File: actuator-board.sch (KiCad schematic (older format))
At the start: 29 parts, among them J5 SWD/DEBUG, J6 BATTERY, J7 CAN, J8 CAN, U1 STM32F302K8U6, U2 MCP1703, U3 MAX3051, X1 16MHz 10ppm

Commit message: layout: power electronics, more components on F.Cu layer
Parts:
- U2: footprint Package_TO_SOT_SMD:SOT-23_Handsoldering -> Package_TO_SOT_SMD:SOT-23
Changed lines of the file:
@@
 F 0 "U2" H 9100 1200 60  0000 C CNN
 F 1 "MCP1703" H 8800 1200 60  0000 C CNN
-F 2 "Package_TO_SOT_SMD:SOT-23_Handsoldering" H 8750 1450 60  0001 C CNN
+F 2 "Package_TO_SOT_SMD:SOT-23" H 8750 1450 60  0001 C CNN
 F 3 "" H 8750 1450 60  0000 C CNN
 F 4 "MCP1703T-3302E/CBCT-ND" H 8850 1300 50  0001 C CNN "digikey#"

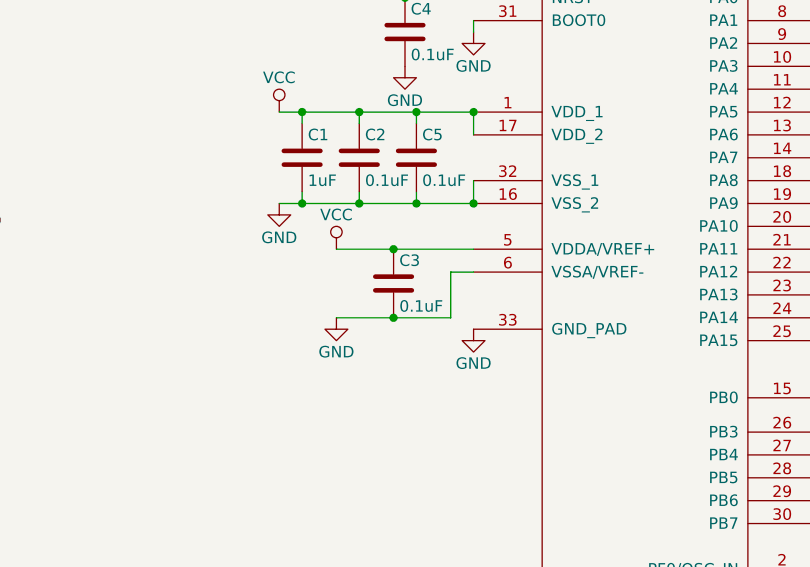
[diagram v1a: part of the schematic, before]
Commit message: HTSSOP motor driver, component arrangment, added MCU capacitor
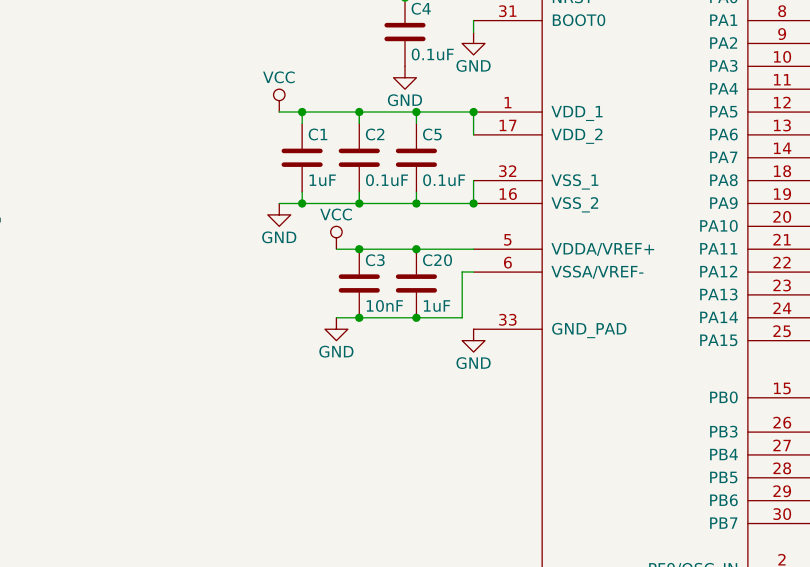
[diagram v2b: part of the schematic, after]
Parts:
- added C20: 1uF, Capacitor_SMD:C_0603_1608Metric, symbol Device:C
- C3: value 0.1uF -> 10nF
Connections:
- net GND: now also C20.2
- net VCC: now also C20.1
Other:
- moved on the sheet: C3
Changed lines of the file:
@@
-$EndComp
-$Comp
-L Device:C C3
-U 1 1 56D6293B
-P 3500 4350
-F 0 "C3" H 3525 4450 50  0000 L CNN
-F 1 "0.1uF" H 3525 4250 50  0000 L CNN
-F 2 "Capacitor_SMD:C_0603_1608Metric" H 3538 4200 50  0001 C CNN
-F 3 "" H 3500 4350 50  0000 C CNN
-	1    3500 4350
-	1    0    0    -1
 $EndComp
 $Comp
@@
 	2150 1600 1750 1600
 Wire Wire Line
-	3750 4300 3750 4500
-Wire Wire Line
-	3850 4300 3750 4300
+	3800 4300 3800 4500
+Wire Wire Line
+	3850 4300 3800 4300
 Connection ~ 3350 4000
 Wire Wire Line
@@
 Wire Wire Line
 	3400 3100 3550 3100
-Wire Wire Line
-	3250 4500 3500 4500
-Wire Wire Line
-	3250 4200 3500 4200
 Wire Wire Line
 	5350 3700 5450 3700
@@
 	1    0    0    -1
 $EndComp
-Connection ~ 3500 4200
-Wire Wire Line
-	3500 4200 3850 4200
-Connection ~ 3500 4500
-Wire Wire Line
-	3500 4500 3750 4500
 $Comp
 L power:GND #PWR012
@@
 Text Label 5450 3100 0    60   ~ 0
 ANALOG1
+$Comp
+L Device:C C20
+U 1 1 5E52DAB3
+P 3600 4350
+F 0 "C20" H 3625 4450 50  0000 L CNN
+F 1 "1uF" H 3625 4250 50  0000 L CNN
+F 2 "Capacitor_SMD:C_0603_1608Metric" H 3638 4200 50  0001 C CNN
+F 3 "" H 3600 4350 50  0000 C CNN
+	1    3600 4350
+	1    0    0    -1
+$EndComp
+Connection ~ 3600 4200
+Wire Wire Line
+	3600 4200 3850 4200
+Connection ~ 3600 4500
+Wire Wire Line
+	3600 4500 3800 4500
+Wire Wire Line
+	3250 4500 3350 4500
+Connection ~ 3350 4500
+Wire Wire Line
+	3350 4500 3600 4500
+Wire Wire Line
+	3250 4200 3350 4200
+Connection ~ 3350 4200
+Wire Wire Line
+	3350 4200 3600 4200
+$Comp
+L Device:C C3
+U 1 1 56D6293B
+P 3350 4350
+F 0 "C3" H 3375 4450 50  0000 L CNN
+F 1 "10nF" H 3375 4250 50  0000 L CNN
+F 2 "Capacitor_SMD:C_0603_1608Metric" H 3388 4200 50  0001 C CNN
+F 3 "" H 3350 4350 50  0000 C CNN
+	1    3350 4350
+	1    0    0    -1
+$EndComp
 $EndSCHEMATC

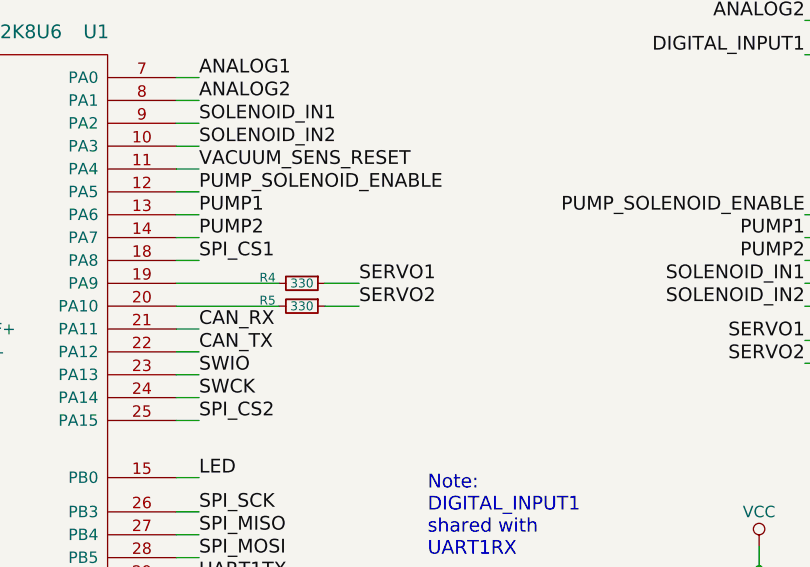
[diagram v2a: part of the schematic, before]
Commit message: Silk screen doc, ground vias, exchange servo 1 <-> 2
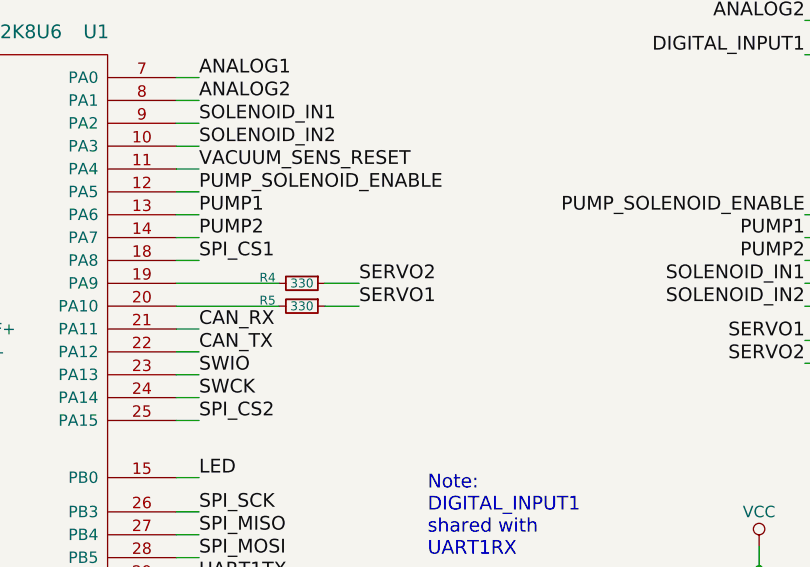
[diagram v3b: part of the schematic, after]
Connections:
- net SERVO1: now also R5.1; no longer R4.1
- net SERVO2: now also R4.1; no longer R5.1
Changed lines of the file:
@@
-	1    0    0    -1
-$EndComp
-$Comp
-L _logo:CVRA_logo #G1
-U 1 1 5BCDA49A
-P 10150 6850
-F 0 "#G1" H 10150 6682 60  0001 C CNN
-F 1 "CVRA_logo" H 10150 7018 60  0001 C CNN
-F 2 "_logo:CVRA-logo-small" H 10150 6850 50  0001 C CNN
-F 3 "" H 10150 6850 50  0001 C CNN
-	1    10150 6850
 	1    0    0    -1
 $EndComp
@@
 Wire Wire Line
 	5450 3200 5350 3200
-Text Label 6150 4000 0    60   ~ 0
-SERVO1
-Text Label 6150 4100 0    60   ~ 0
-SERVO2
 Text Label 5450 3800 0    60   ~ 0
 PUMP2
@@
 	1    0    0    -1
 $EndComp
+Text Label 6150 4000 0    60   ~ 0
+SERVO2
+Text Label 6150 4100 0    60   ~ 0
+SERVO1
+$Comp
+L _logo:CVRA_logo #G1
+U 1 1 5BCDA49A
+P 10150 6850
+F 0 "#G1" H 10150 6682 60  0001 C CNN
+F 1 "CVRA_logo" H 10150 7018 60  0001 C CNN
+F 2 "_logo:CVRA-logo-small" H 10150 6850 50  0001 C CNN
+F 3 "" H 10150 6850 50  0001 C CNN
+	1    10150 6850
+	1    0    0    -1
+$EndComp

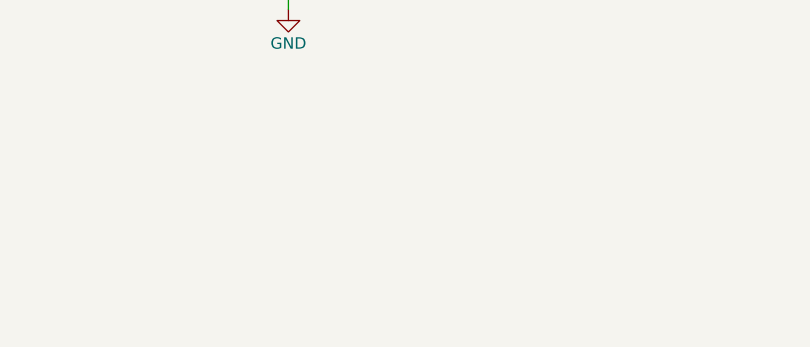
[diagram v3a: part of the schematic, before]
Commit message: Changes from review: move C2, move VCC via, add fiducials, component placement
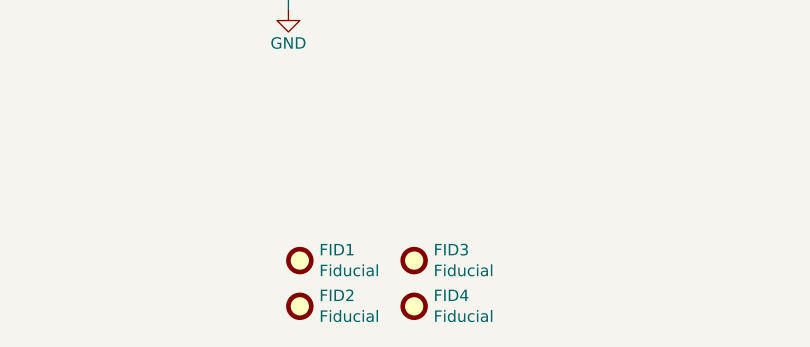
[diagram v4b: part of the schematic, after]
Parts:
- added FID1, FID2, FID3, FID4: Fiducial, Fiducial:Fiducial_0.5mm_Mask1mm, symbol Mechanical:Fiducial
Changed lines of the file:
@@
+	1    0    0    -1
+$EndComp
+$Comp
+L Mechanical:Fiducial FID2
+U 1 1 5E5D272E
+P 6000 7550
+F 0 "FID2" H 6085 7596 50  0000 L CNN
+F 1 "Fiducial" H 6085 7505 50  0000 L CNN
+F 2 "Fiducial:Fiducial_0.5mm_Mask1mm" H 6000 7550 50  0001 C CNN
+F 3 "~" H 6000 7550 50  0001 C CNN
+	1    6000 7550
+	1    0    0    -1
+$EndComp
+$Comp
+L Mechanical:Fiducial FID1
+U 1 1 5E5CBA36
+P 6000 7350
+F 0 "FID1" H 6085 7396 50  0000 L CNN
+F 1 "Fiducial" H 6085 7305 50  0000 L CNN
+F 2 "Fiducial:Fiducial_0.5mm_Mask1mm" H 6000 7350 50  0001 C CNN
+F 3 "~" H 6000 7350 50  0001 C CNN
+	1    6000 7350
+	1    0    0    -1
+$EndComp
+$Comp
+L Mechanical:Fiducial FID4
+U 1 1 5E5EBB2E
+P 6500 7550
+F 0 "FID4" H 6585 7596 50  0000 L CNN
+F 1 "Fiducial" H 6585 7505 50  0000 L CNN
+F 2 "Fiducial:Fiducial_0.5mm_Mask1mm" H 6500 7550 50  0001 C CNN
+F 3 "~" H 6500 7550 50  0001 C CNN
+	1    6500 7550
+	1    0    0    -1
+$EndComp
+$Comp
+L Mechanical:Fiducial FID3
+U 1 1 5E5EBB38
+P 6500 7350
+F 0 "FID3" H 6585 7396 50  0000 L CNN
+F 1 "Fiducial" H 6585 7305 50  0000 L CNN
+F 2 "Fiducial:Fiducial_0.5mm_Mask1mm" H 6500 7350 50  0001 C CNN
+F 3 "~" H 6500 7350 50  0001 C CNN
+	1    6500 7350
 	1    0    0    -1
 $EndComp

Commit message: Update DigiKey references
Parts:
- C1, C10, C20: digikey# (none) -> 399-3118-1-ND
- C2, C4, C5, C8: digikey# (none) -> 399-1283-1-ND
- C3: digikey# (none) -> 399-1092-1-ND
- C7: digikey# (none) -> 399-17563-1-ND
- C9: digikey# 399-11133-1-ND -> 399-3118-1-ND
- FID1, FID2, FID3, FID4: DNP (none) -> 1
- R5, R6: digikey# (none) -> 311-330HRCT-ND
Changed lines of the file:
@@
 F 2 "Capacitor_SMD:C_0603_1608Metric" H 7488 5250 50  0001 C CNN
 F 3 "" H 7450 5400 50  0000 C CNN
+F 4 "399-1283-1-ND" H 7450 5400 50  0001 C CNN "digikey#"
 	1    7450 5400
 	1    0    0    -1
@@
 F 2 "Capacitor_SMD:C_0603_1608Metric" H 3638 3650 50  0001 C CNN
 F 3 "" H 3600 3800 50  0000 C CNN
+F 4 "399-1283-1-ND" H 3600 3800 50  0001 C CNN "digikey#"
 	1    3600 3800
 	1    0    0    -1
@@
 F 2 "Capacitor_SMD:C_0603_1608Metric" H 3138 3650 50  0001 C CNN
 F 3 "" H 3100 3800 50  0000 C CNN
+F 4 "399-3118-1-ND" H 3100 3800 50  0001 C CNN "digikey#"
 	1    3100 3800
 	1    0    0    -1
@@
 F 2 "Capacitor_SMD:C_0603_1608Metric" H 3388 3650 50  0001 C CNN
 F 3 "" H 3350 3800 50  0000 C CNN
+F 4 "399-1283-1-ND" H 3350 3800 50  0001 C CNN "digikey#"
 	1    3350 3800
 	1    0    0    -1
@@
 F 2 "Capacitor_SMD:C_0603_1608Metric" H 3588 3100 50  0001 C CNN
 F 3 "" H 3550 3250 50  0000 C CNN
+F 4 "399-1283-1-ND" H 3550 3250 50  0001 C CNN "digikey#"
 	1    3550 3250
 	1    0    0    -1
@@
 F 2 "Capacitor_SMD:C_0603_1608Metric" H 6338 5850 50  0001 C CNN
 F 3 "" H 6300 6000 50  0000 C CNN
+F 4 "399-17563-1-ND" H 6300 6000 50  0001 C CNN "digikey#"
 	1    6300 6000
 	1    0    0    -1
@@
 F 2 "Capacitor_SMD:C_0603_1608Metric" H 9488 1050 50  0001 C CNN
 F 3 "" H 9450 1200 50  0000 C CNN
+F 4 "399-3118-1-ND" H 9450 1200 50  0001 C CNN "digikey#"
 	1    9450 1200
 	1    0    0    -1
@@
 F 2 "Capacitor_SMD:C_0603_1608Metric" H 8288 1050 50  0001 C CNN
 F 3 "" H 8250 1200 50  0000 C CNN
-F 4 "399-11133-1-ND" H 8250 1200 50  0001 C CNN "digikey#"
+F 4 "399-3118-1-ND" H 8250 1200 50  0001 C CNN "digikey#"
 	1    8250 1200
 	1    0    0    -1
@@
 F 2 "Resistor_SMD:R_0603_1608Metric" H 5900 4100 50  0001 C CNN
 F 3 "~" H 5900 4100 50  0001 C CNN
+F 4 "311-330HRCT-ND" H 5900 4100 50  0001 C CNN "digikey#"
 	1    5900 4100
 	0    1    1    0
@@
 F 2 "Resistor_SMD:R_0603_1608Metric" H 6100 5400 50  0001 C CNN
 F 3 "~" H 6100 5400 50  0001 C CNN
+F 4 "311-330HRCT-ND" H 6100 5400 50  0001 C CNN "digikey#"
 	1    6100 5400
 	0    1    1    0
@@
 F 2 "Capacitor_SMD:C_0603_1608Metric" H 3638 4200 50  0001 C CNN
 F 3 "" H 3600 4350 50  0000 C CNN
+F 4 "399-3118-1-ND" H 3600 4350 50  0001 C CNN "digikey#"
 	1    3600 4350
 	1    0    0    -1
@@
 F 2 "Capacitor_SMD:C_0603_1608Metric" H 3388 4200 50  0001 C CNN
 F 3 "" H 3350 4350 50  0000 C CNN
+F 4 "399-1092-1-ND" H 3350 4350 50  0001 C CNN "digikey#"
 	1    3350 4350
 	1    0    0    -1
@@
 F 2 "Fiducial:Fiducial_0.5mm_Mask1mm" H 6000 7550 50  0001 C CNN
 F 3 "~" H 6000 7550 50  0001 C CNN
+F 4 "1" H 6000 7550 50  0001 C CNN "DNP"
 	1    6000 7550
 	1    0    0    -1
@@
 F 2 "Fiducial:Fiducial_0.5mm_Mask1mm" H 6000 7350 50  0001 C CNN
 F 3 "~" H 6000 7350 50  0001 C CNN
+F 4 "1" H 6000 7350 50  0001 C CNN "DNP"
 	1    6000 7350
 	1    0    0    -1
@@
 F 2 "Fiducial:Fiducial_0.5mm_Mask1mm" H 6500 7550 50  0001 C CNN
 F 3 "~" H 6500 7550 50  0001 C CNN
+F 4 "1" H 6500 7550 50  0001 C CNN "DNP"
 	1    6500 7550
 	1    0    0    -1
@@
 F 2 "Fiducial:Fiducial_0.5mm_Mask1mm" H 6500 7350 50  0001 C CNN
 F 3 "~" H 6500 7350 50  0001 C CNN
+F 4 "1" H 6500 7350 50  0001 C CNN "DNP"
 	1    6500 7350
 	1    0    0    -1
